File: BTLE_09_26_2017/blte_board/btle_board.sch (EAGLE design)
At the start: 13 parts, among them P3 USB-B1HSB6, P4 POWER_JACKPTH, P9 44764-1201

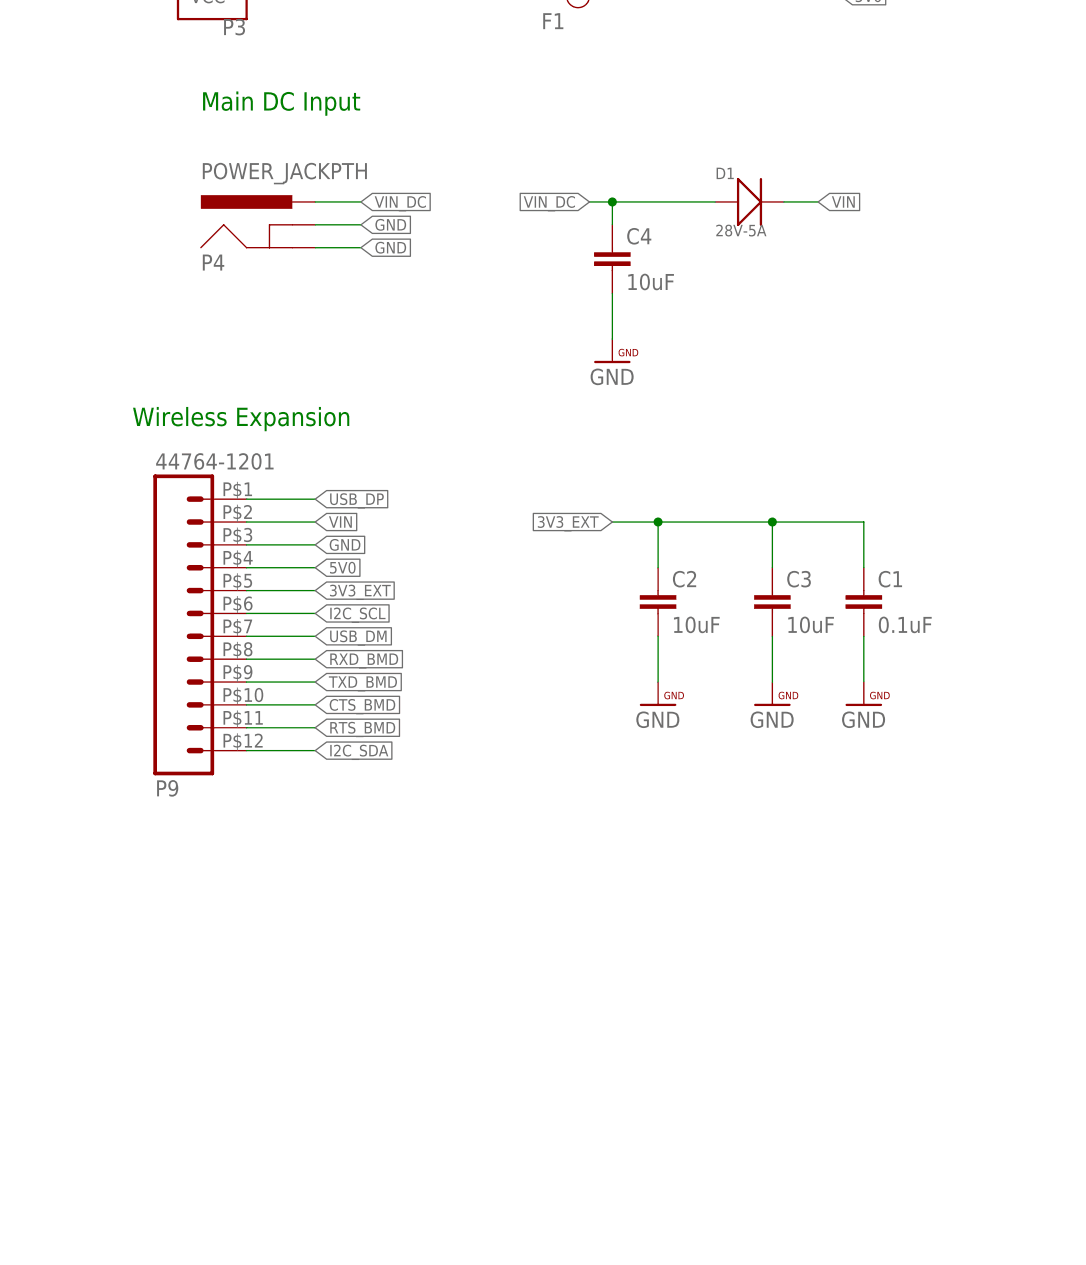
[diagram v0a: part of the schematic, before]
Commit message: Add Battery & Mounting Holes to BLTE board
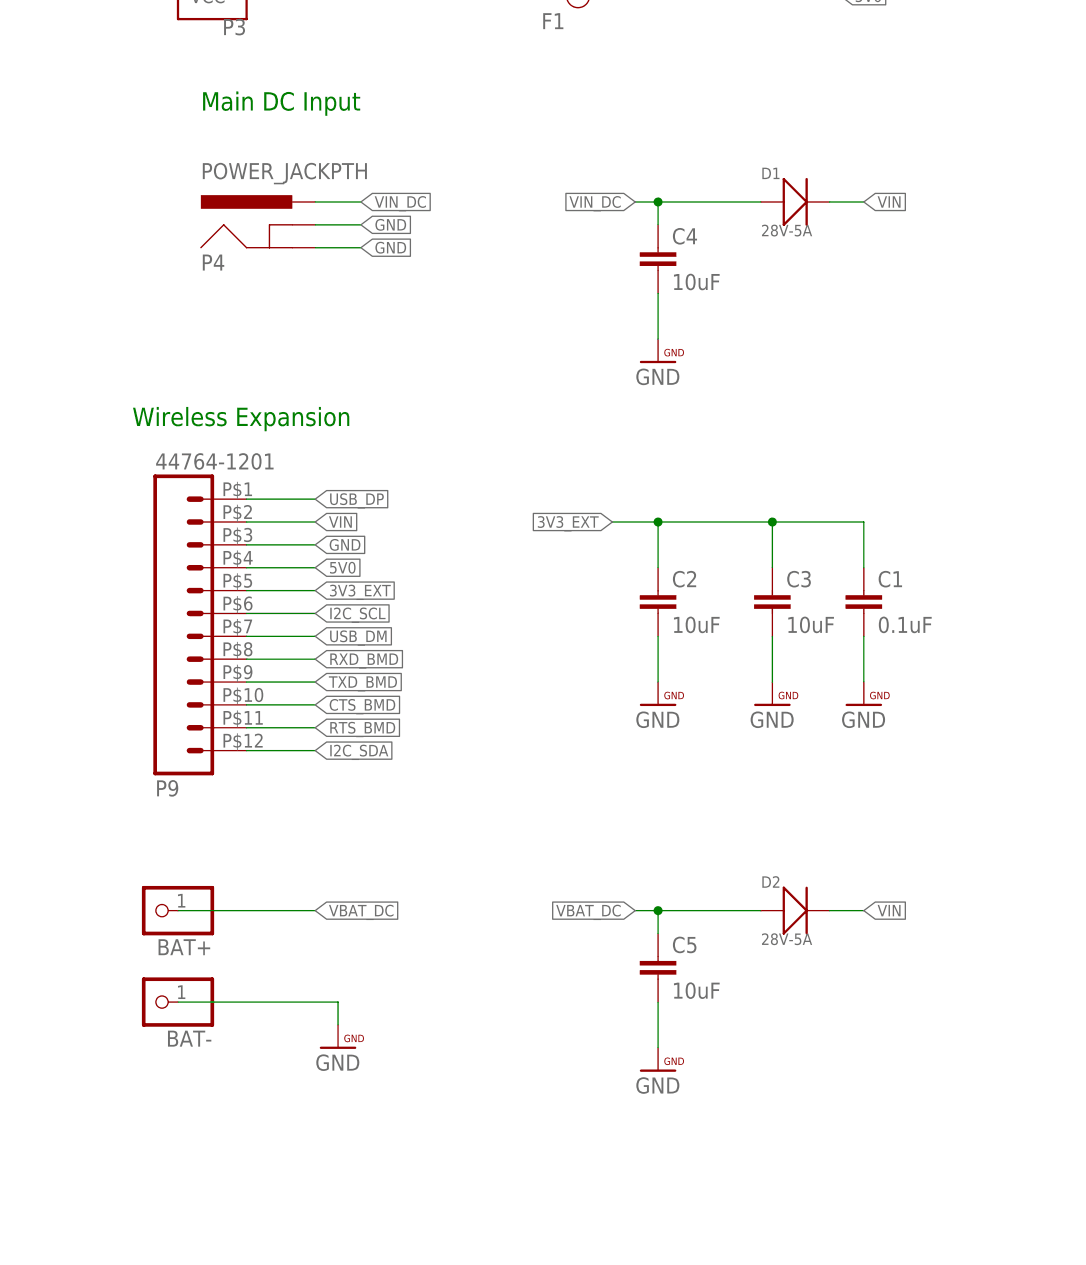
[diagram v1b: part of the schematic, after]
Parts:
- added BAT+, BAT-: (no value), PatternAgents-ProtoPads:WPAD-1-PTH
- added C5: 10uF, PatternAgents-ProtoPads:CAP0603-CAP
- added D2: 28V-5A, Seeed-Diode-2016:SMD-DIODE-SCHOTTKY-28V-5A(DO-214AA)
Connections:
- new net VBAT_DC: BAT+.1, C5.1, D2.+
- net GND: now also BAT-.1, C5.2
- net VIN: now also D2.-
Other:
- moved on the sheet: C4, D1
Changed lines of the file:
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@@
 <setting verticaltext="up"/>
 </settings>
-<grid distance="0.1" unitdist="inch" unit="inch" style="lines" multiple="1" display="no" altdistance="0.01" altunitdist="inch" altunit="inch"/>
+<grid distance="0.1" unitdist="inch" unit="inch" style="dots" multiple="1" display="yes" altdistance="0.01" altunitdist="inch" altunit="inch"/>
 <layers>
 <layer number="1" name="Top" color="4" fill="1" visible="no" active="no"/>
@@
 <part name="R1" library="PatternAgents-ProtoPads" deviceset="RESISTOR" device="0402-TYP" value="470"/>
 <part name="U$21" library="PatternAgents-Beautify" deviceset="GND" device=""/>
+<part name="C5" library="PatternAgents-ProtoPads" deviceset="CAP" device="0603-CAP" value="10uF"/>
+<part name="U$4" library="PatternAgents-Beautify" deviceset="GND" device=""/>
+<part name="D2" library="Seeed-Diode-2016" deviceset="SMD-DIODE-SCHOTTKY-28V-5A(DO-214AA)" device="" value="28V-5A"/>
+<part name="BAT+" library="PatternAgents-ProtoPads" deviceset="WPAD-1" device="-PTH"/>
+<part name="BAT-" library="PatternAgents-ProtoPads" deviceset="WPAD-1" device="-PTH"/>
+<part name="U$5" library="PatternAgents-Beautify" deviceset="GND" device=""/>
 </parts>
 <sheets>
@@
 <instance part="P1" gate="G$1" x="256.54" y="167.64"/>
 <instance part="P4" gate="G$1" x="38.1" y="139.7"/>
-<instance part="C4" gate="G$1" x="73.66" y="139.7"/>
-<instance part="U$15" gate="G$1" x="73.66" y="132.08"/>
+<instance part="C4" gate="G$1" x="78.74" y="139.7"/>
+<instance part="U$15" gate="G$1" x="78.74" y="132.08"/>
 <instance part="F1" gate="A" x="63.5" y="170.18" smashed="yes">
 <attribute name="NAME" x="65.7606" y="166.5224" size="1.778" layer="95" ratio="10" rot="SR0"/>
 </instance>
 <instance part="P3" gate="G$1" x="33.02" y="172.72" rot="R180"/>
-<instance part="D1" gate="G$1" x="88.9" y="147.32"/>
+<instance part="D1" gate="G$1" x="93.98" y="147.32"/>
 <instance part="C3" gate="G$1" x="91.44" y="101.6"/>
 <instance part="U$1" gate="G$1" x="91.44" y="93.98"/>
@@
 <instance part="R1" gate="R" x="251.46" y="142.24" rot="R90"/>
 <instance part="U$21" gate="G$1" x="259.08" y="132.08"/>
+<instance part="C5" gate="G$1" x="78.74" y="60.96"/>
+<instance part="U$4" gate="G$1" x="78.74" y="53.34"/>
+<instance part="D2" gate="G$1" x="93.98" y="68.58"/>
+<instance part="BAT+" gate="G$1" x="22.86" y="68.58" rot="R180"/>
+<instance part="BAT-" gate="G$1" x="22.86" y="58.42" rot="R180"/>
+<instance part="U$5" gate="G$1" x="43.18" y="55.88"/>
 </instances>
 <busses>
@@
 <segment>
 <pinref part="C4" gate="G$1" pin="2"/>
-<wire x1="73.66" y1="137.16" x2="73.66" y2="132.08" width="0.1524" layer="91"/>
+<wire x1="78.74" y1="137.16" x2="78.74" y2="132.08" width="0.1524" layer="91"/>
 <pinref part="U$15" gate="G$1" pin="GND"/>
 </segment>
@@
 <wire x1="259.08" y1="134.62" x2="259.08" y2="132.08" width="0.1524" layer="91"/>
 <pinref part="U$21" gate="G$1" pin="GND"/>
+</segment>
+<segment>
+<pinref part="C5" gate="G$1" pin="2"/>
+<wire x1="78.74" y1="58.42" x2="78.74" y2="53.34" width="0.1524" layer="91"/>
+<pinref part="U$4" gate="G$1" pin="GND"/>
+</segment>
+<segment>
+<wire x1="25.4" y1="58.42" x2="43.18" y2="58.42" width="0.1524" layer="91"/>
+<pinref part="U$5" gate="G$1" pin="GND"/>
+<wire x1="43.18" y1="58.42" x2="43.18" y2="55.88" width="0.1524" layer="91"/>
+<pinref part="BAT-" gate="G$1" pin="1"/>
 </segment>
 </net>
@@
 <segment>
 <pinref part="C4" gate="G$1" pin="1"/>
-<label x="71.12" y="147.32" size="1.27" layer="95" font="vector" ratio="10" rot="R180" xref="yes"/>
-<wire x1="85.09" y1="147.32" x2="73.66" y2="147.32" width="0.1524" layer="91"/>
-<wire x1="73.66" y1="147.32" x2="71.12" y2="147.32" width="0.1524" layer="91"/>
-<wire x1="73.66" y1="144.78" x2="73.66" y2="147.32" width="0.1524" layer="91"/>
-<junction x="73.66" y="147.32"/>
+<label x="76.2" y="147.32" size="1.27" layer="95" font="vector" ratio="10" rot="R180" xref="yes"/>
+<wire x1="90.17" y1="147.32" x2="78.74" y2="147.32" width="0.1524" layer="91"/>
+<wire x1="78.74" y1="147.32" x2="76.2" y2="147.32" width="0.1524" layer="91"/>
+<wire x1="78.74" y1="144.78" x2="78.74" y2="147.32" width="0.1524" layer="91"/>
+<junction x="78.74" y="147.32"/>
 <pinref part="D1" gate="G$1" pin="+"/>
 </segment>
@@
 <net name="VIN" class="0">
 <segment>
-<label x="96.52" y="147.32" size="1.27" layer="95" font="vector" ratio="10" xref="yes"/>
+<label x="101.6" y="147.32" size="1.27" layer="95" font="vector" ratio="10" xref="yes"/>
 <pinref part="D1" gate="G$1" pin="-"/>
-<wire x1="92.71" y1="147.32" x2="96.52" y2="147.32" width="0.1524" layer="91"/>
+<wire x1="97.79" y1="147.32" x2="101.6" y2="147.32" width="0.1524" layer="91"/>
 </segment>
 <segment>
@@
 <label x="40.64" y="111.76" size="1.27" layer="95" font="vector" ratio="10" rot="MR180" xref="yes"/>
 <pinref part="P9" gate="G$1" pin="2"/>
+</segment>
+<segment>
+<label x="101.6" y="68.58" size="1.27" layer="95" font="vector" ratio="10" xref="yes"/>
+<pinref part="D2" gate="G$1" pin="-"/>
+<wire x1="97.79" y1="68.58" x2="101.6" y2="68.58" width="0.1524" layer="91"/>
 </segment>
 </net>
@@
 </segment>
 </net>
+<net name="VBAT_DC" class="0">
+<segment>
+<pinref part="C5" gate="G$1" pin="1"/>
+<label x="76.2" y="68.58" size="1.27" layer="95" font="vector" ratio="10" rot="R180" xref="yes"/>
+<wire x1="90.17" y1="68.58" x2="78.74" y2="68.58" width="0.1524" layer="91"/>
+<wire x1="78.74" y1="68.58" x2="76.2" y2="68.58" width="0.1524" layer="91"/>
+<wire x1="78.74" y1="66.04" x2="78.74" y2="68.58" width="0.1524" layer="91"/>
+<junction x="78.74" y="68.58"/>
+<pinref part="D2" gate="G$1" pin="+"/>
+</segment>
+<segment>
+<wire x1="25.4" y1="68.58" x2="40.64" y2="68.58" width="0.1524" layer="91"/>
+<label x="40.64" y="68.58" size="1.27" layer="95" ratio="10" xref="yes"/>
+<pinref part="BAT+" gate="G$1" pin="1"/>
+</segment>
+</net>
